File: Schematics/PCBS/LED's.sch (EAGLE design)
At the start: 3 parts

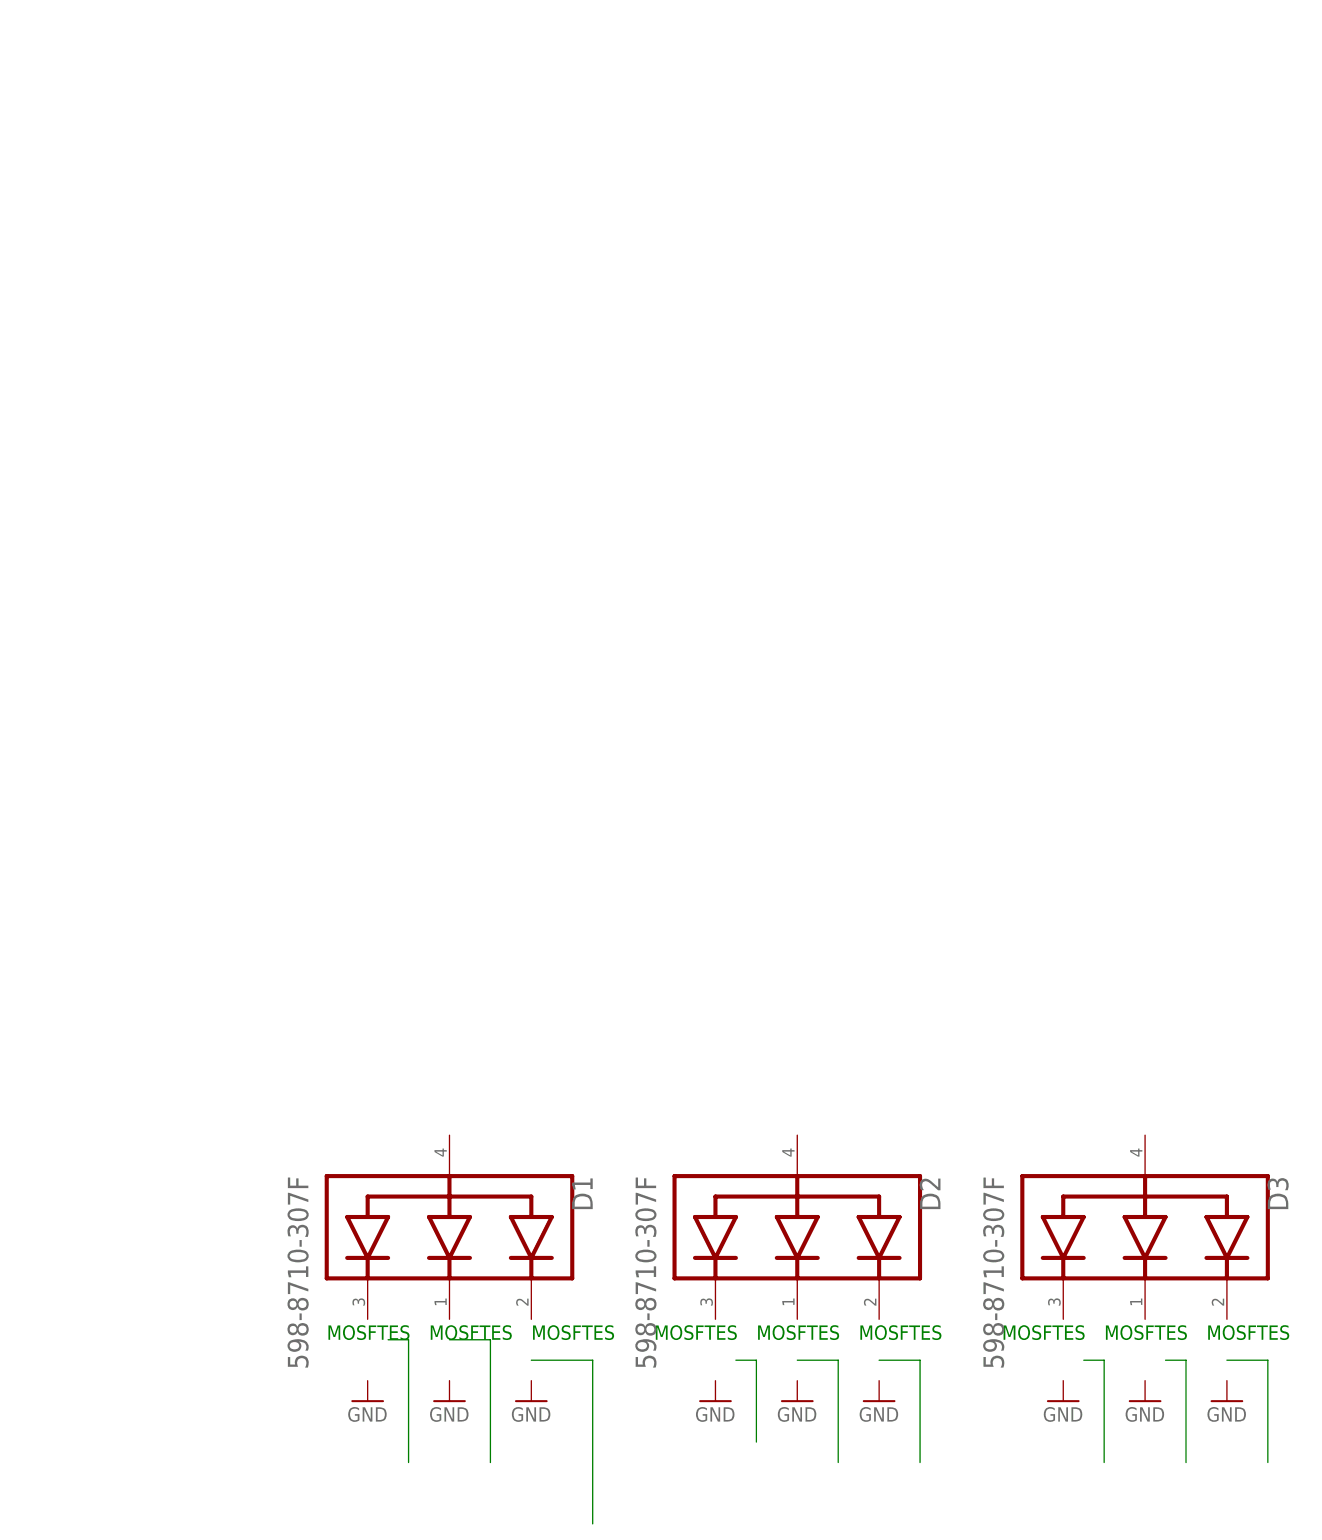
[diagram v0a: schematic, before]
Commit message: led + atmega328
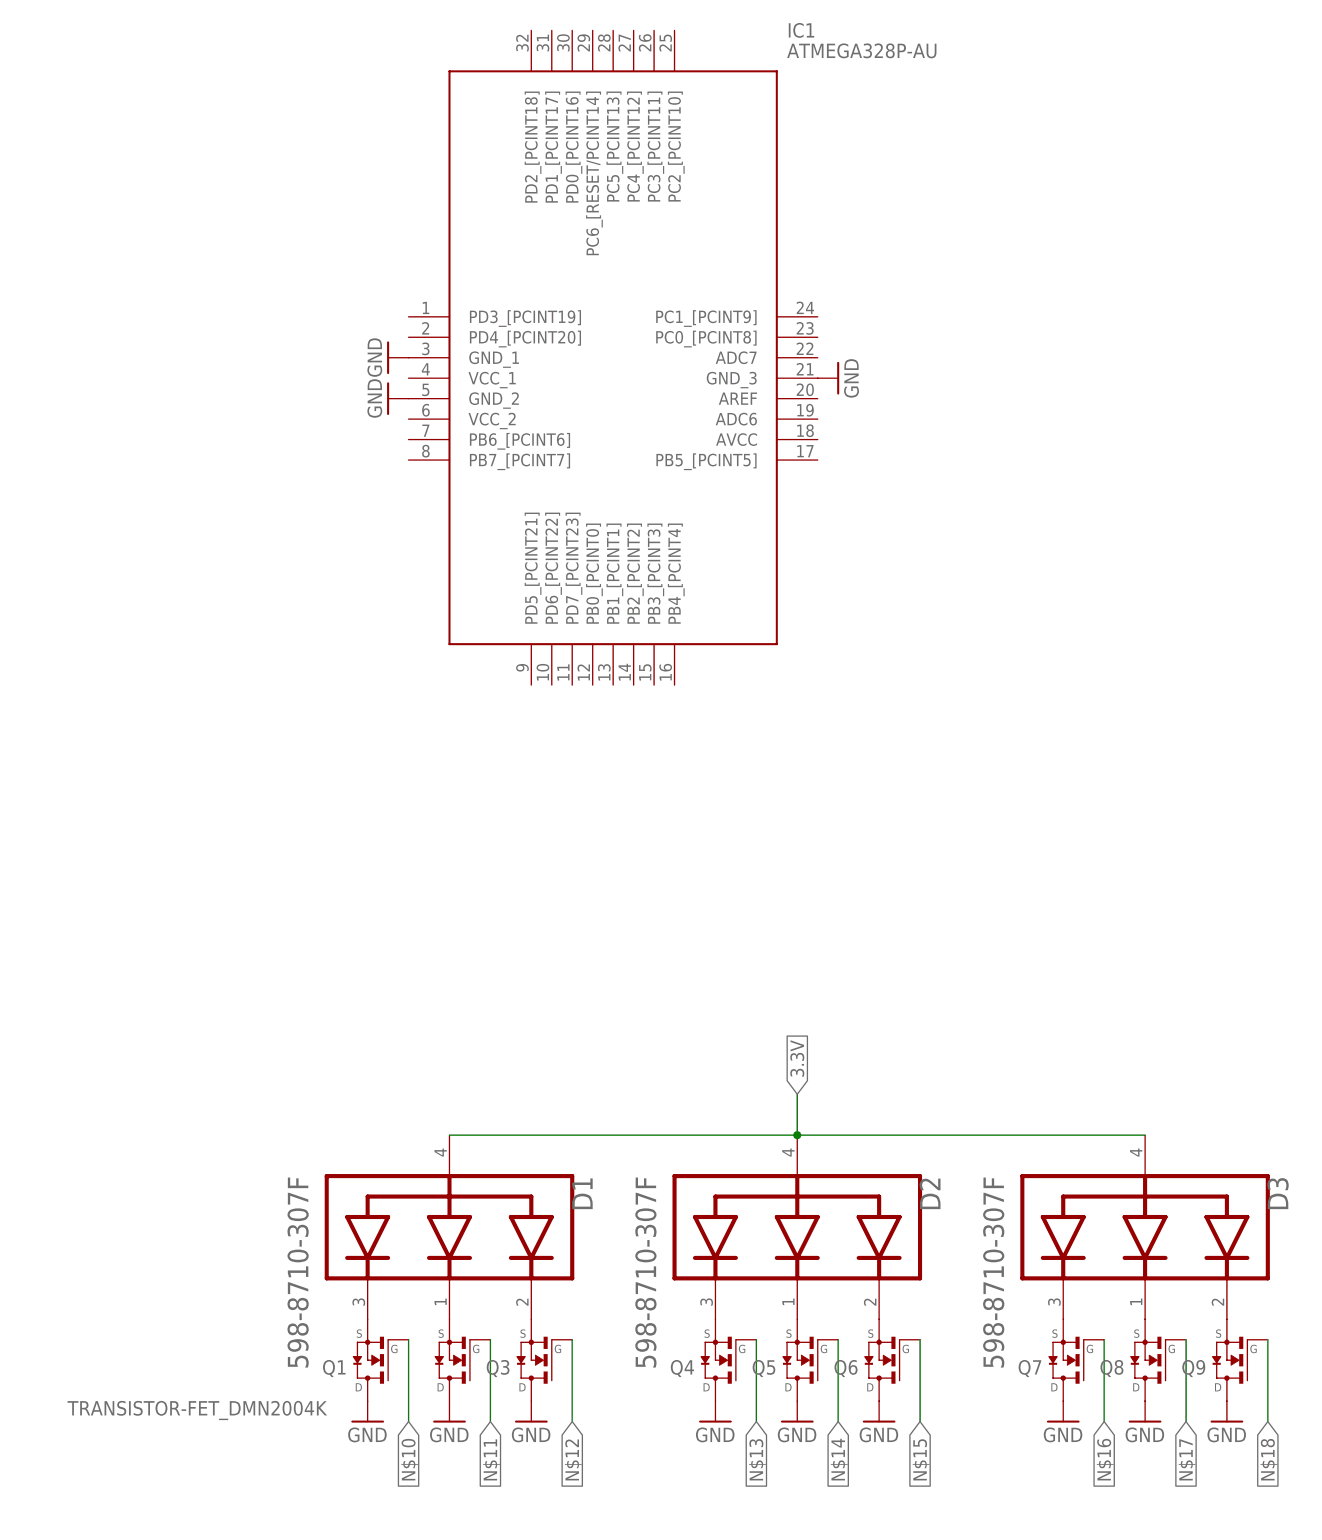
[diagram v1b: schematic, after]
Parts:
- added IC1: ATMEGA328P-AU, ATMEGA328P-AU:ATMEGA328P-AU
- added Q1, Q2, Q3, Q4, Q5, Q6, Q7, Q8, Q9: TRANSISTOR-FET_DMN2004K, 52101-101-REV-A:TRANSISTOR-FET_DMN2004K
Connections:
- new net 3.3V: D1.COMMON_ANODE, D2.COMMON_ANODE, D3.COMMON_ANODE
- new net GND: IC1.GND_1, IC1.GND_2, IC1.GND_3, Q1.D, Q2.D, Q3.D, Q4.D, Q5.D, Q6.D, Q7.D, Q8.D, Q9.D
- new net N$1: D1.BLUE_CATHODE, Q1.S
- new net N$10: Q1.G
- new net N$11: Q2.G
- new net N$12: Q3.G
- new net N$13: Q4.G
- new net N$14: Q5.G
- new net N$15: Q6.G
- new net N$16: Q7.G
- new net N$17: Q8.G
- new net N$18: Q9.G
- new net N$2: D1.GREEN_CATHODE, Q2.S
- new net N$3: D1.RED_CATHODE, Q3.S
- new net N$4: D2.BLUE_CATHODE, Q4.S
- new net N$5: D2.GREEN_CATHODE, Q5.S
- new net N$6: D2.RED_CATHODE, Q6.S
- new net N$7: D3.BLUE_CATHODE, Q7.S
- new net N$8: D3.GREEN_CATHODE, Q8.S
- new net N$9: D3.RED_CATHODE, Q9.S
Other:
- note removed: "MOSFTES"
